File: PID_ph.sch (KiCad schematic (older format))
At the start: 40 parts

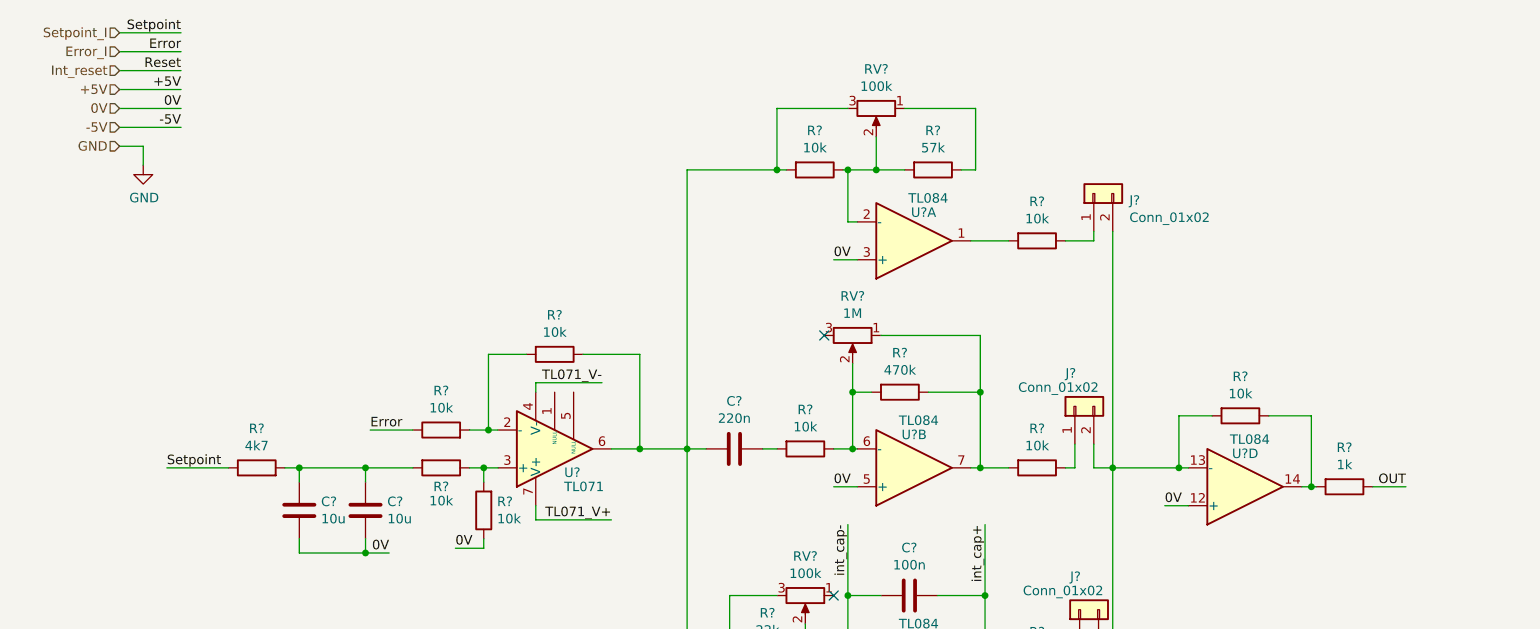
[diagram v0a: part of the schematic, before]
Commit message: Added laser diode, power stage, connecting block in progress
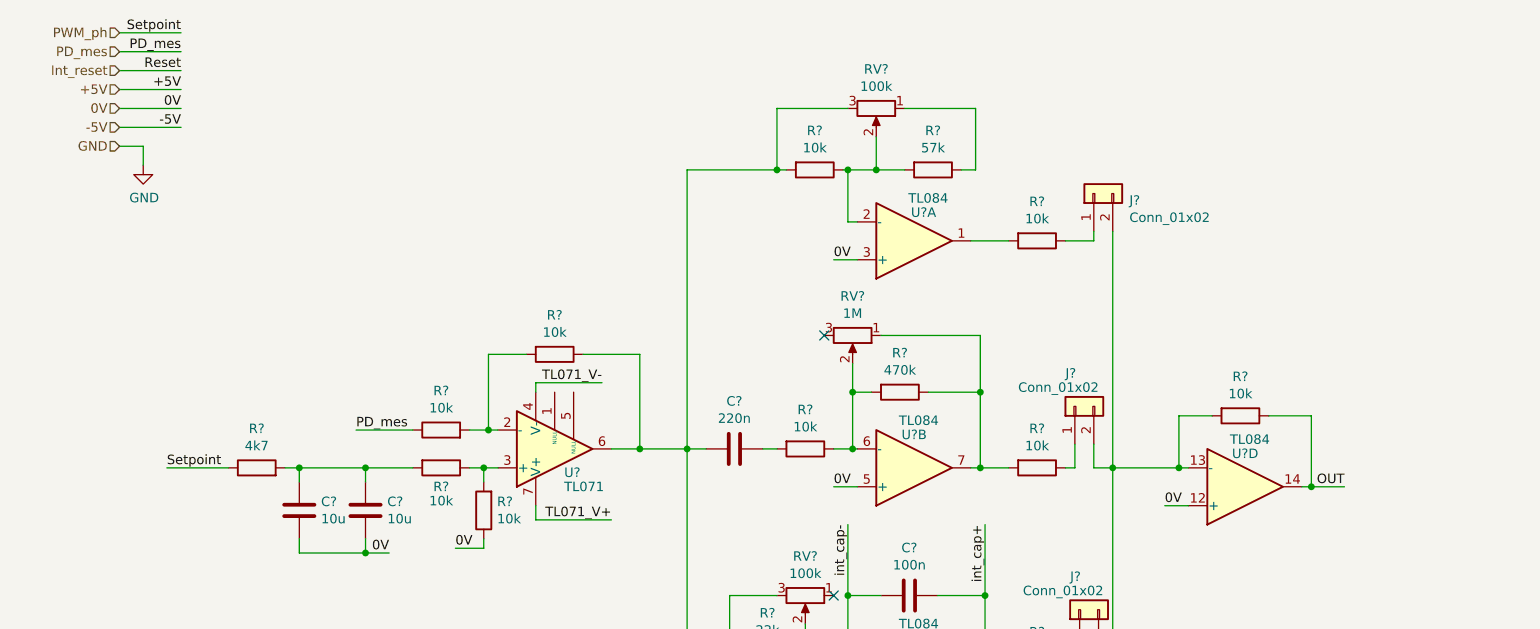
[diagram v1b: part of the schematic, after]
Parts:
- removed R?: 1k, symbol Device:R
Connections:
- net OUT: now also R?.1, U?.14
- net Error_I renamed PD_mes
- net Setpoint_I renamed PWM_ph
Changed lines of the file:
@@
 $Descr A4 11693 8268
 encoding utf-8
-Sheet 12 12
+Sheet 11 11
 Title ""
 Date ""
@@
 $EndComp
 Text HLabel 950  600  0    50   Input ~ 0
-Setpoint_I
+PWM_ph
 Text HLabel 950  700  0    50   Input ~ 0
-Error_I
+PD_mes
 Text HLabel 950  900  0    50   Input ~ 0
 +5V
@@
 Wire Wire Line
 	6475 3100 6600 3100
-$Comp
-L Device:R R?
-U 1 1 619938D0
-P 7425 3000
-AR Path="/619B51F3/619938D0" Ref="R?"  Part="1"
-AR Path="/61820F6B/619938D0" Ref="R?"  Part="1"
-AR Path="/61A28785/619938D0" Ref="R?"  Part="1"
-AR Path="/61A63B19/619938D0" Ref="R?"  Part="1"
-AR Path="/619BC68D/619938D0" Ref="R?"  Part="1"
-AR Path="/619C27A2/619938D0" Ref="R?"  Part="1"
-AR Path="/619C2E9F/619938D0" Ref="R?"  Part="1"
-AR Path="/619C995F/619938D0" Ref="R?"  Part="1"
-F 0 "R?" V 7218 3000 50  0000 C CNN
-F 1 "1k" V 7309 3000 50  0000 C CNN
-F 2 "" V 7355 3000 50  0001 C CNN
-F 3 "~" H 7425 3000 50  0001 C CNN
-	1    7425 3000
-	0    1    1    0
-$EndComp
-Wire Wire Line
-	7275 3000 7250 3000
 Connection ~ 7250 3000
-Text Label 7750 3000 2    50   ~ 0
+Text Label 7425 3000 2    50   ~ 0
 OUT
-Wire Wire Line
-	7750 3000 7575 3000
 Text Label 10550 675  0    50   ~ 0
 OUT
@@
 Wire Wire Line
 	1275 600  950  600
-Text Label 1275 700  2    50   ~ 0
-Error
 Wire Wire Line
 	1275 700  950  700
-Text Label 2275 2700 0    50   ~ 0
-Error
+Text Label 2200 2700 0    50   ~ 0
+PD_mes
 Text Label 1200 2900 0    50   ~ 0
 Setpoint
@@
 Wire Wire Line
 	950  1100 1275 1100
-Wire Wire Line
-	2275 2700 2500 2700
 $Comp
 L Device:C C?
@@
 Wire Wire Line
 	3850 5375 4150 5375
+Wire Wire Line
+	7250 3000 7425 3000
+Text Label 1275 700  2    50   ~ 0
+PD_mes
+Wire Wire Line
+	2200 2700 2500 2700
 $EndSCHEMATC
